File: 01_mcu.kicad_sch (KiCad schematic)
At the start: 3 parts, among them J2 UART, J3 SWD, U1 Pico

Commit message: fix selfcontained and kibot output
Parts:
- U1: footprint RPi_Pico:RPi_Pico_SMD_TH -> prj-footprints:RPi_Pico_SMD_TH
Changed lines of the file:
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@@
 			)
 		)
-		(property "Footprint" "RPi_Pico:RPi_Pico_SMD_TH"
+		(property "Footprint" "prj-footprints:RPi_Pico_SMD_TH"
 			(at 142.24 77.47 90)
 			(effects

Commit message: switched to self-contained symbols, update kibot conf
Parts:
- removed U1: Pico, prj-footprints:RPi_Pico_SMD_TH, symbol MCU_RaspberryPi:Pico
- added U3: Pico, RPi_Pico:RPi_Pico_SMD_TH, symbol MCU_RaspberryPi_and_Boards:Pico
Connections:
- net +3.3V: now also U3.36 (3V3)
- net BTN_1: now also U3.4 (GPIO2)
- net BTN_2: now also U3.5 (GPIO3)
- net BTN_3: now also U3.6 (GPIO4)
- net BTN_4: now also U3.7 (GPIO5)
- net EPD_BUSY: now also U3.29 (GPIO22)
- net EPD_CS: now also U3.22 (GPIO17)
- net EPD_DC: now also U3.26 (GPIO20)
- net EPD_DIN: now also U3.25 (GPIO19)
- net EPD_RST: now also U3.27 (GPIO21)
- net EPD_SCK: now also U3.24 (GPIO18)
- net GND: now also U3.13 (GND), U3.18 (GND), U3.23 (GND), U3.28 (GND), U3.3 (GND), U3.33 (AGND), U3.38 (GND), U3.42 (GND), U3.8 (GND)
- net SD_CLK-SCLK: now also U3.14 (GPIO10)
- net SD_CMD-DI: now also U3.15 (GPIO11)
- net SD_DAT0-DO: now also U3.16 (GPIO12)
- net SD_DAT3-CD-CS: now also U3.17 (GPIO13)
- net VBUS: now also U3.40 (VBUS)
- net VSYS: now also U3.39 (VSYS)
- net at J3.1 (Pin_1): now also U3.43 (SWDIO)
- net at J3.3 (Pin_3): now also U3.41 (SWCLK)
- net at J2.1 (Pin_1): now also U3.1 (GPIO0)
- net at J2.2 (Pin_2): now also U3.2 (GPIO1)
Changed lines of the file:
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@@
+	)
+	(symbol
+		(lib_id "MCU_RaspberryPi_and_Boards:Pico")
+		(at 142.24 77.47 0)
+		(unit 1)
+		(exclude_from_sim no)
+		(in_bom yes)
+		(on_board yes)
+		(dnp no)
+		(fields_autoplaced yes)
+		(property "Reference" "U3"
+			(at 142.24 45.72 0)
+			(effects
+				(font
+					(size 1.27 1.27)
+				)
+			)
+		)
+		(property "Value" "Pico"
+			(at 142.24 48.26 0)
+			(effects
+				(font
+					(size 1.27 1.27)
+				)
+			)
+		)
+		(property "Footprint" "RPi_Pico:RPi_Pico_SMD_TH"
+			(at 142.24 77.47 90)
+			(effects
+				(font
+					(size 1.27 1.27)
+				)
+				(hide yes)
+			)
+		)
+		(property "Datasheet" ""
+			(at 142.24 77.47 0)
+			(effects
+				(font
+					(size 1.27 1.27)
+				)
+				(hide yes)
+			)
+		)
+		(property "Description" ""
+			(at 142.24 77.47 0)
+			(effects
+				(font
+					(size 1.27 1.27)
+				)
+				(hide yes)
+			)
+		)
+		(pin "23"
+		)
+		(pin "24"
+		)
+		(pin "25"
+		)
+		(pin "26"
+		)
+		(pin "11"
+		)
+		(pin "21"
+		)
+		(pin "14"
+		)
+		(pin "29"
+		)
+		(pin "3"
+		)
+		(pin "17"
+		)
+		(pin "1"
+		)
+		(pin "15"
+		)
+		(pin "36"
+		)
+		(pin "37"
+		)
+		(pin "38"
+		)
+		(pin "39"
+		)
+		(pin "4"
+		)
+		(pin "40"
+		)
+		(pin "41"
+		)
+		(pin "42"
+		)
+		(pin "43"
+		)
+		(pin "5"
+		)
+		(pin "6"
+		)
+		(pin "7"
+		)
+		(pin "8"
+		)
+		(pin "9"
+		)
+		(pin "22"
+		)
+		(pin "30"
+		)
+		(pin "31"
+		)
+		(pin "32"
+		)
+		(pin "13"
+		)
+		(pin "16"
+		)
+		(pin "10"
+		)
+		(pin "27"
+		)
+		(pin "28"
+		)
+		(pin "20"
+		)
+		(pin "19"
+		)
+		(pin "18"
+		)
+		(pin "2"
+		)
+		(pin "12"
+		)
+		(pin "33"
+		)
+		(pin "34"
+		)
+		(pin "35"
+		)
+		(instances
+			(project ""
+				(path "/ec954637-2a8b-4662-b4a1-f88107f11cb0/8ebc337b-62e9-431a-9c7d-4f5ee75e8f92"
+					(reference "U3")
+					(unit 1)
+				)
+			)
+		)
 	)
 	(symbol
@@
 					(unit 1)
 				)
-			)
-		)
-	)
-	(symbol
-		(lib_id "MCU_RaspberryPi:Pico")
-		(at 142.24 77.47 0)
-		(unit 1)
-		(exclude_from_sim no)
-		(in_bom yes)
-		(on_board yes)
-		(dnp no)
-		(fields_autoplaced yes)
-		(property "Reference" "U1"
-			(at 142.24 45.72 0)
-			(effects
-				(font
-					(size 1.27 1.27)
-				)
-			)
-		)
-		(property "Value" "Pico"
-			(at 142.24 48.26 0)
-			(effects
-				(font
-					(size 1.27 1.27)
-				)
-			)
-		)
-		(property "Footprint" "prj-footprints:RPi_Pico_SMD_TH"
-			(at 142.24 77.47 90)
-			(effects
-				(font
-					(size 1.27 1.27)
-				)
-				(hide yes)
-			)
-		)
-		(property "Datasheet" ""
-			(at 142.24 77.47 0)
-			(effects
-				(font
-					(size 1.27 1.27)
-				)
-				(hide yes)
-			)
-		)
-		(property "Description" ""
-			(at 142.24 77.47 0)
-			(effects
-				(font
-					(size 1.27 1.27)
-				)
-				(hide yes)
-			)
-		)
-		(pin "17"
-		)
-		(pin "1"
-		)
-		(pin "16"
-		)
-		(pin "10"
-		)
-		(pin "2"
-		)
-		(pin "20"
-		)
-		(pin "23"
-		)
-		(pin "24"
-		)
-		(pin "29"
-		)
-		(pin "3"
-		)
-		(pin "30"
-		)
-		(pin "31"
-		)
-		(pin "11"
-		)
-		(pin "18"
-		)
-		(pin "12"
-		)
-		(pin "40"
-		)
-		(pin "41"
-		)
-		(pin "42"
-		)
-		(pin "34"
-		)
-		(pin "35"
-		)
-		(pin "14"
-		)
-		(pin "4"
-		)
-		(pin "27"
-		)
-		(pin "28"
-		)
-		(pin "36"
-		)
-		(pin "37"
-		)
-		(pin "19"
-		)
-		(pin "38"
-		)
-		(pin "39"
-		)
-		(pin "32"
-		)
-		(pin "33"
-		)
-		(pin "15"
-		)
-		(pin "13"
-		)
-		(pin "43"
-		)
-		(pin "5"
-		)
-		(pin "6"
-		)
-		(pin "7"
-		)
-		(pin "8"
-		)
-		(pin "9"
-		)
-		(pin "25"
-		)
-		(pin "26"
-		)
-		(pin "21"
-		)
-		(pin "22"
-		)
-		(instances
-			(project ""
-				(path "/ec954637-2a8b-4662-b4a1-f88107f11cb0/8ebc337b-62e9-431a-9c7d-4f5ee75e8f92"
-					(reference "U1")
-					(unit 1)
-				)

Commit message: fix selfcontainment issues, added 2D rendering
Signed-off-by: Anna-Lena Marx <anna-lena.marx@web.de>
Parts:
- U3: footprint RPi_Pico:RPi_Pico_SMD_TH -> prj-footprints:RPi_Pico_SMD_TH
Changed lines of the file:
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@@
 			)
 		)
-		(property "Footprint" "RPi_Pico:RPi_Pico_SMD_TH"
+		(property "Footprint" "prj-footprints:RPi_Pico_SMD_TH"
 			(at 142.24 77.47 90)
 			(effects

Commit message: Imported Aisler design rules, routed power and display booster
Signed-off-by: Anna-Lena Marx <anna-lena.marx@web.de>
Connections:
- net GND: now also J2.1 (Pin_1); no longer J2.3 (Pin_3)
- net at U3.1 (GPIO0): now also J2.3 (Pin_3); no longer J2.1 (Pin_1)
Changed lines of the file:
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@@
+		)
+	)
+	(netclass_flag ""
+		(length 2.54)
+		(shape round)
+		(at 180.34 63.5 0)
+		(fields_autoplaced yes)
+		(effects
+			(font
+				(size 1.27 1.27)
+			)
+			(justify left bottom)
+		)
+		(property "Netclass" "PWR"
+			(at 181.0385 60.96 0)
+			(effects
+				(font
+					(size 1.27 1.27)
+					(italic yes)
+				)
+				(justify left)
+			)
 		)
 	)
@@
 		(lib_id "Connector:Conn_01x03_Pin")
 		(at 113.03 55.88 0)
+		(mirror x)
 		(unit 1)
 		(exclude_from_sim no)
@@
 		(dnp no)
 		(property "Reference" "J2"
-			(at 116.586 46.736 0)
+			(at 116.586 65.024 0)
 			(effects
 				(font
@@
 		)
 		(property "Value" "UART"
-			(at 116.84 49.276 0)
-			(effects
-				(font
+			(at 116.84 62.484 0)
+			(effects
+				(font

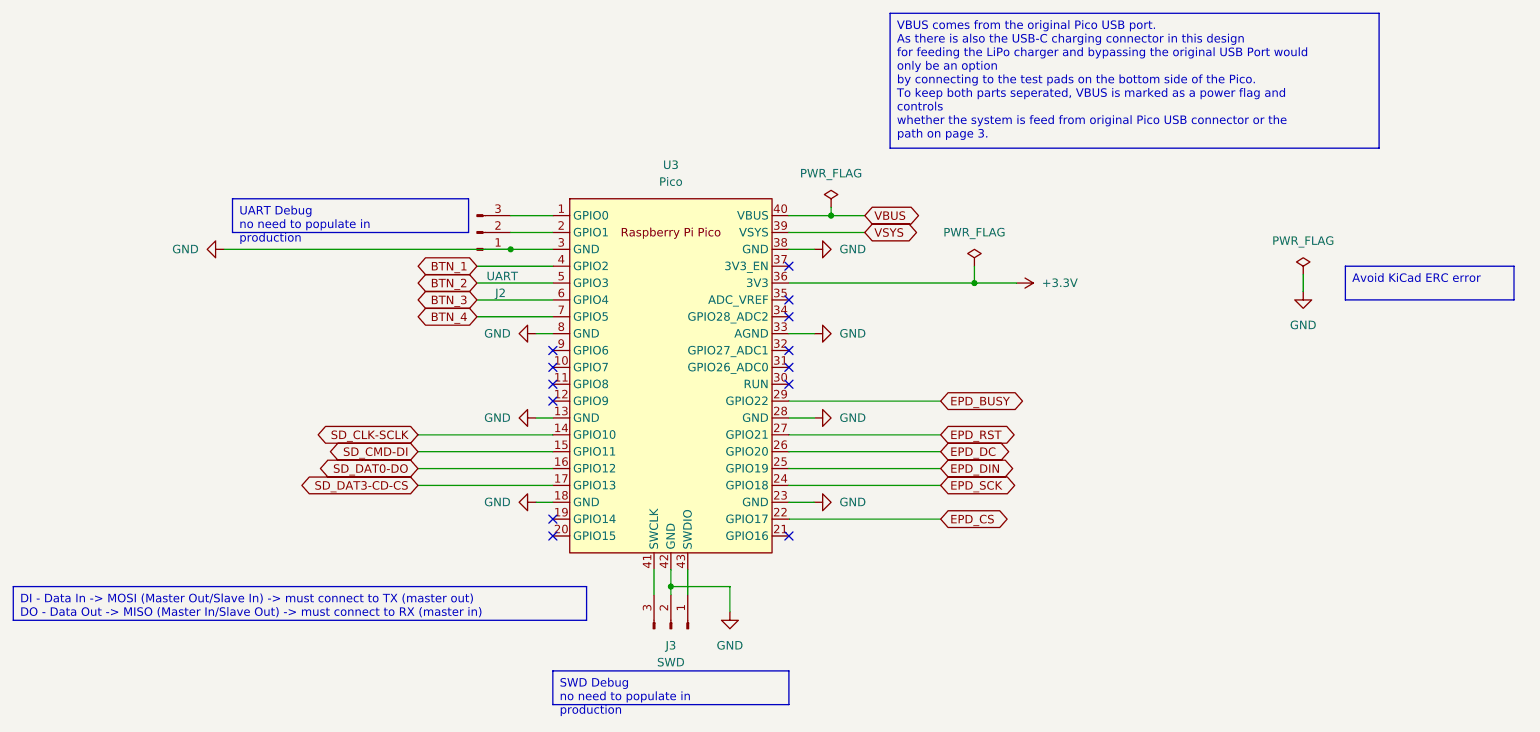
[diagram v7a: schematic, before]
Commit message: Migrate to KiCad 9, start working on the new revision
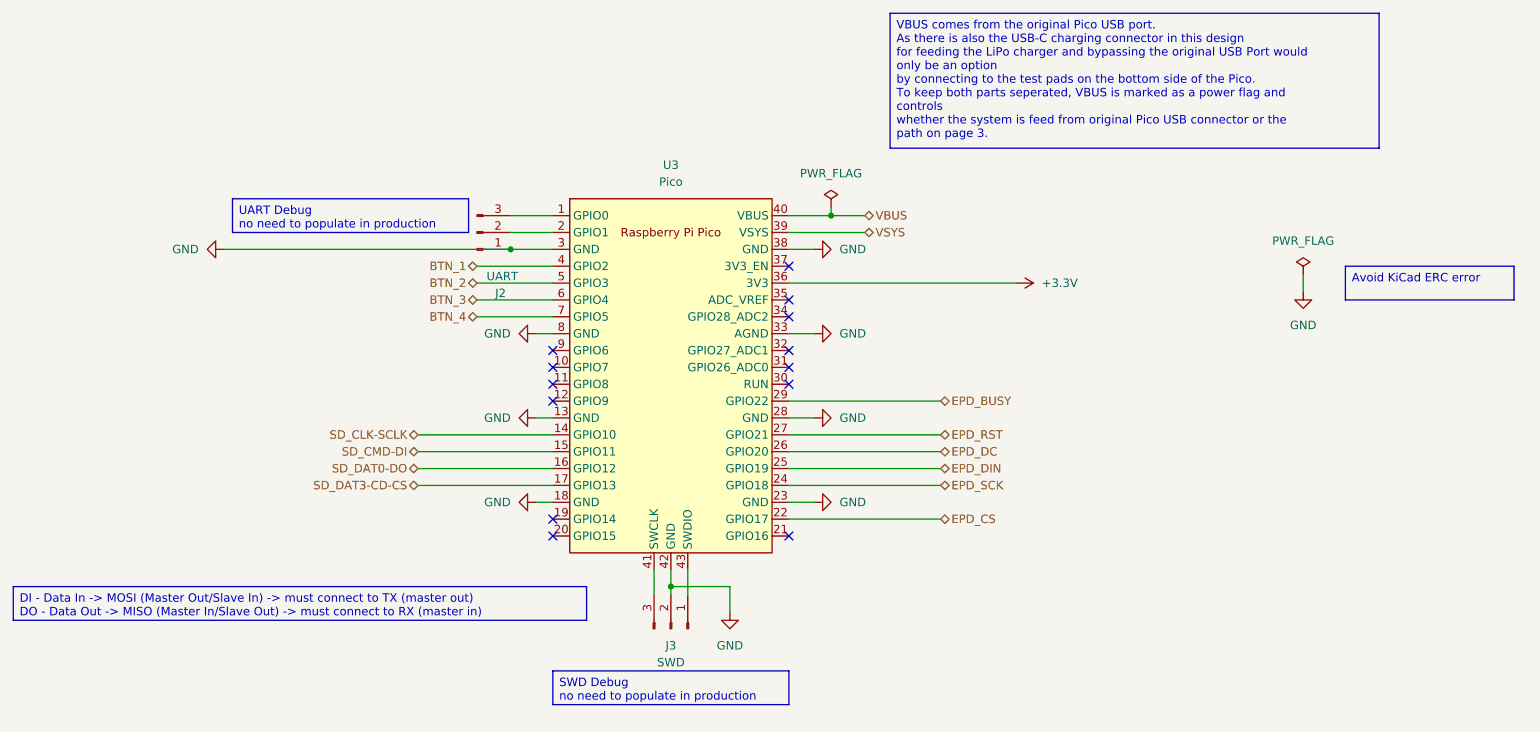
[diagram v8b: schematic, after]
